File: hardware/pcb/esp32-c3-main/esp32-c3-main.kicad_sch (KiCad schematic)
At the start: 8 parts, among them J1 USB-C Receptacle USB2.0 16P

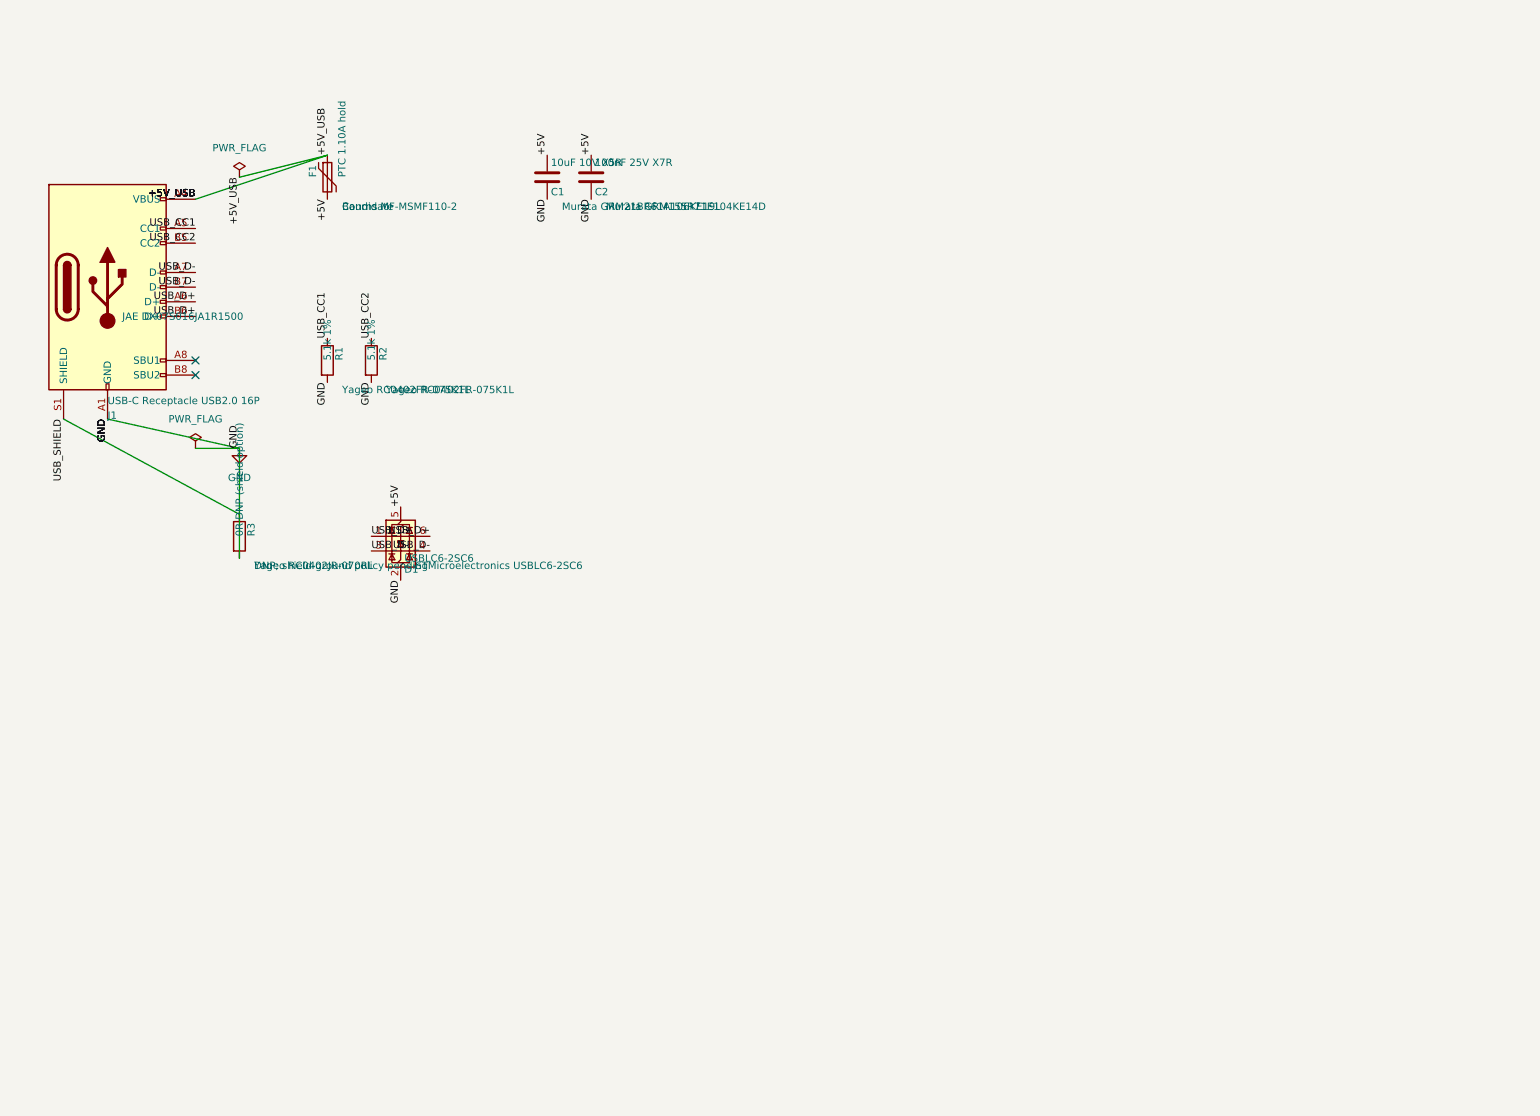
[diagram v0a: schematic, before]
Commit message: Complete ESP32-C3 main schematic
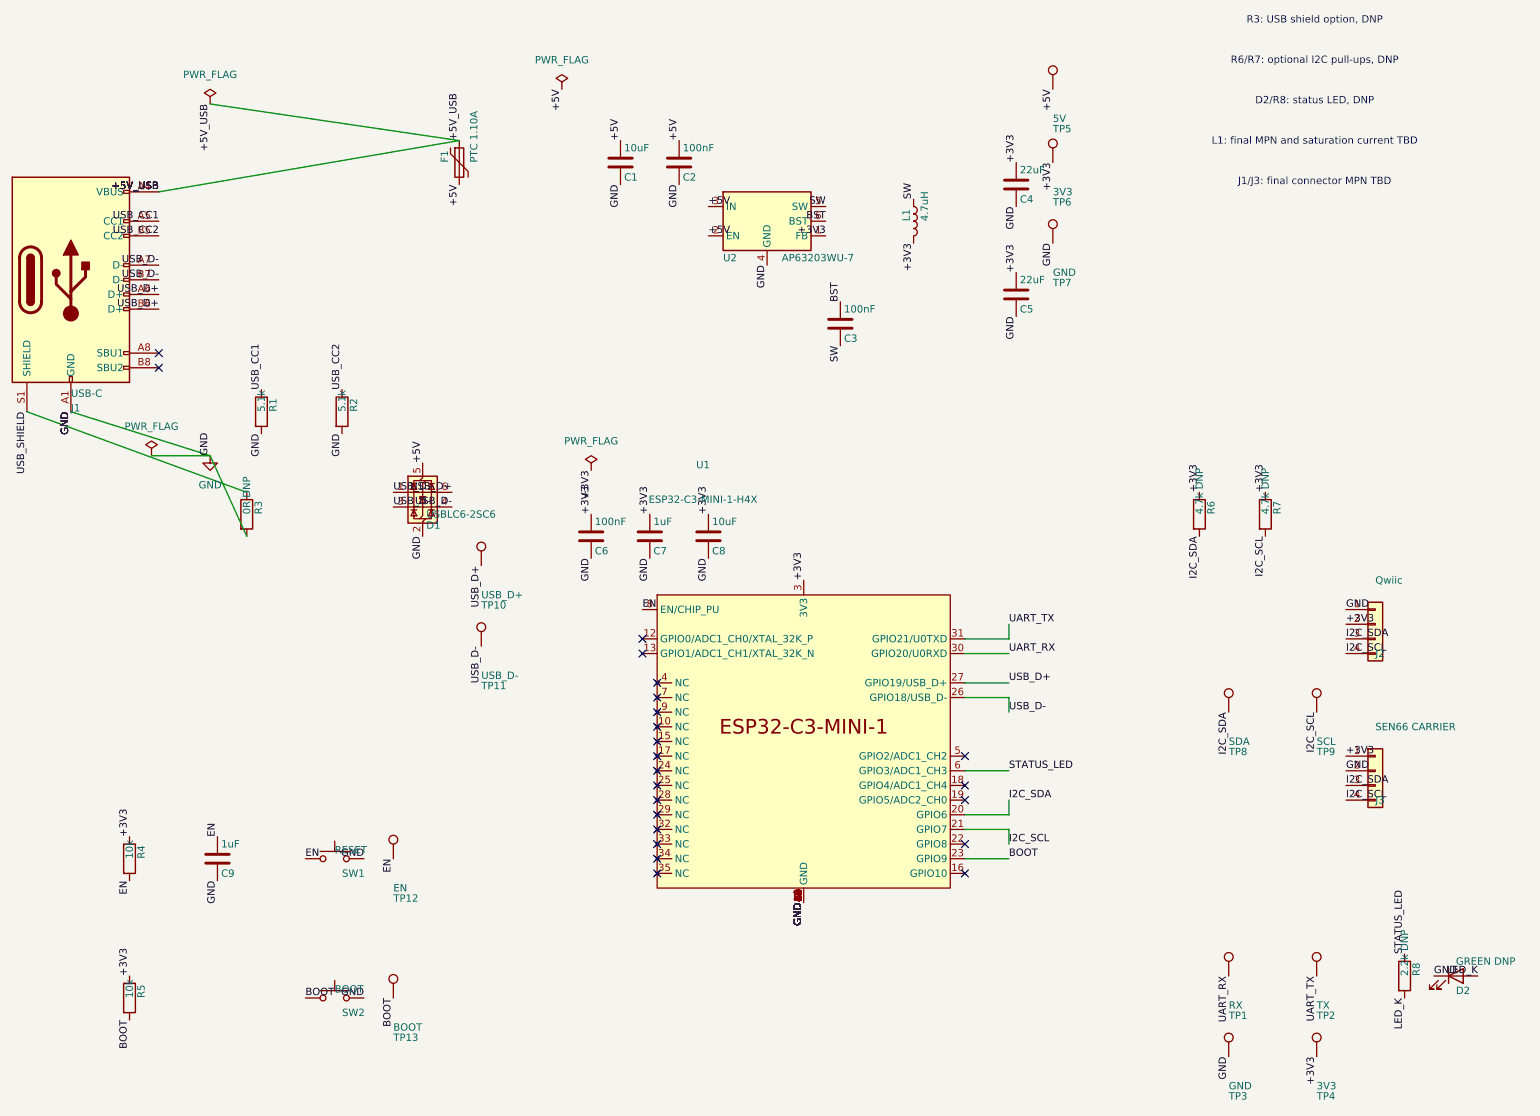
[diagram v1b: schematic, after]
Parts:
- added C3, C6: 100nF, Capacitor_SMD:C_0402_1005Metric, symbol Device:C
- added C4, C5: 22uF, Capacitor_SMD:C_0805_2012Metric, symbol Device:C
- added C7, C9: 1uF, Capacitor_SMD:C_0402_1005Metric, symbol Device:C
- added C8: 10uF, Capacitor_SMD:C_0805_2012Metric, symbol Device:C
- added D2: GREEN DNP, LED_SMD:LED_0603_1608Metric, symbol Device:LED
- added J2: Qwiic, Connector_JST:JST_SH_SM04B-SRSS-TB_1x04-1MP_P1.00mm_Horizontal, symbol Connector_Generic:Conn_01x04
- added J3: SEN66 CARRIER, Connector_PinHeader_2.54mm:PinHeader_1x04_P2.54mm_Horizontal, symbol Connector_Generic:Conn_01x04
- added L1: 4.7uH, Inductor_SMD:L_Vishay_IHLP-2020, symbol Device:L
- added R4, R5: 10k, Resistor_SMD:R_0402_1005Metric, symbol Device:R
- added R6, R7: 4.7k DNP, Resistor_SMD:R_0402_1005Metric, symbol Device:R
- added R8: 2.2k DNP, Resistor_SMD:R_0402_1005Metric, symbol Device:R
- added SW1: RESET, Button_Switch_SMD:SW_SPST_B3U-1000P, symbol Switch:SW_Push
- added SW2: BOOT, Button_Switch_SMD:SW_SPST_B3U-1000P, symbol Switch:SW_Push
- added TP1: RX, TestPoint:TestPoint_Pad_D2.0mm, symbol Connector:TestPoint
- added TP10: USB_D+, TestPoint:TestPoint_Pad_D2.0mm, symbol Connector:TestPoint
- added TP11: USB_D-, TestPoint:TestPoint_Pad_D2.0mm, symbol Connector:TestPoint
- added TP12: EN, TestPoint:TestPoint_Pad_D2.0mm, symbol Connector:TestPoint
- added TP13: BOOT, TestPoint:TestPoint_Pad_D2.0mm, symbol Connector:TestPoint
- added TP2: TX, TestPoint:TestPoint_Pad_D2.0mm, symbol Connector:TestPoint
- added TP3, TP7: GND, TestPoint:TestPoint_Pad_D2.0mm, symbol Connector:TestPoint
- added TP4, TP6: 3V3, TestPoint:TestPoint_Pad_D2.0mm, symbol Connector:TestPoint
- added TP5: 5V, TestPoint:TestPoint_Pad_D2.0mm, symbol Connector:TestPoint
- added TP8: SDA, TestPoint:TestPoint_Pad_D2.0mm, symbol Connector:TestPoint
- added TP9: SCL, TestPoint:TestPoint_Pad_D2.0mm, symbol Connector:TestPoint
- added U1: ESP32-C3-MINI-1-H4X, Espressif:ESP32-C3-MINI-1, symbol Espressif:ESP32-C3-MINI-1
- added U2: AP63203WU-7, Package_TO_SOT_SMD:TSOT-23-6, symbol Regulator_Switching:AP63203WU
- C1: value 10uF 10V X5R -> 10uF
- C2: value 100nF 25V X7R -> 100nF
- D1: LCSC (none) -> C7519
- F1: value PTC 1.10A hold -> PTC 1.10A; Status Candidate -> Candidate; JLC verification required
- J1: value USB-C Receptacle USB2.0 16P -> USB-C; LCSC (none) -> TBD
- R1, R2: value 5.1k 1% -> 5.1k
- R3: value 0R DNP (shield option) -> 0R DNP; Status DNP; shield-ground policy pending -> DNP
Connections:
- net +5V: now also TP5.1, U2.2 (EN), U2.3 (IN)
- net GND: now also C4.2, C5.2, C6.2, C7.2, C8.2, C9.2, D2.1 (K), J2.1 (Pin_1), J3.2 (Pin_2), SW1.2, SW2.2, TP3.1, TP7.1, U1.1 (GND), U1.11 (GND), U1.14 (GND), U1.2 (GND), U1.36 (GND), U1.37 (GND), U1.38 (GND), U1.39 (GND), U1.40 (GND), U1.41 (GND), U1.42 (GND), U1.43 (GND), U1.44 (GND), U1.45 (GND), U1.46 (GND), U1.47 (GND), U1.48 (GND), U1.49 (GND), U1.50 (GND), U1.51 (GND), U1.52 (GND), U1.53 (GND), U2.4 (GND)
- net USB_D+: now also TP10.1, U1.27 (GPIO19/USB_D+)
- net USB_D-: now also TP11.1, U1.26 (GPIO18/USB_D-)
- new net +3V3: C4.1, C5.1, C6.1, C7.1, C8.1, J2.2 (Pin_2), J3.1 (Pin_1), L1.2, R4.1, R5.1, R6.1, R7.1, TP4.1, TP6.1, U1.3 (3V3), U2.1 (FB)
- new net BOOT: R5.2, SW2.1, TP13.1, U1.23 (GPIO9)
- new net BST: C3.1, U2.6 (BST)
- new net EN: C9.1, R4.2, SW1.1, TP12.1, U1.8 (EN/CHIP_PU)
- new net I2C_SCL: J2.4 (Pin_4), J3.4 (Pin_4), R7.2, TP9.1, U1.21 (GPIO7)
- new net I2C_SDA: J2.3 (Pin_3), J3.3 (Pin_3), R6.2, TP8.1, U1.20 (GPIO6)
- new net LED_K: D2.2 (A), R8.2
- new net STATUS_LED: R8.1, U1.6 (GPIO3/ADC1_CH3)
- new net SW: C3.2, L1.1, U2.5 (SW)
- new net UART_RX: TP1.1, U1.30 (GPIO20/U0RXD)
- new net UART_TX: TP2.1, U1.31 (GPIO21/U0TXD)
- no-connect marks 2 -> 23
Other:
- note added: "D2/R8: status LED, DNP"
- note added: "J1/J3: final connector MPN TBD"
- note added: "L1: final MPN and saturation current TBD"
- note added: "R3: USB shield option, DNP"
- note added: "R6/R7: optional I2C pull-ups, DNP"
- company: (none) -> OMK

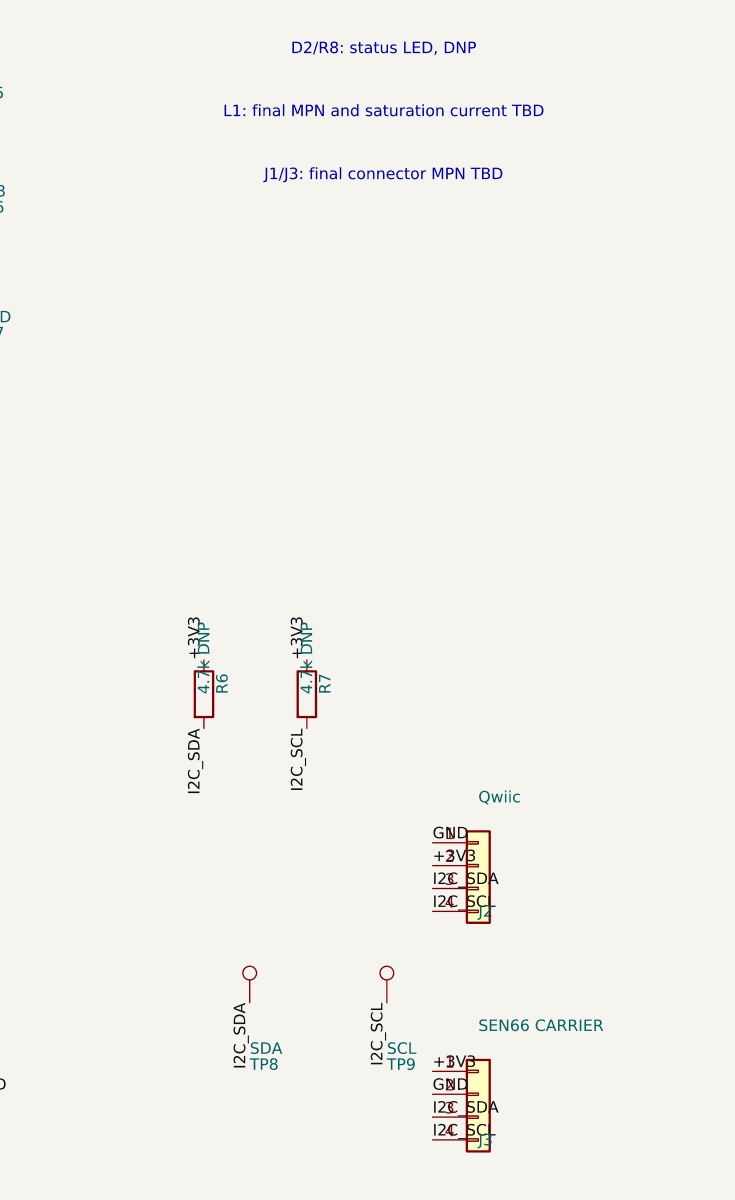
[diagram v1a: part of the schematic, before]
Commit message: Integrate JST PH connectors into schematics
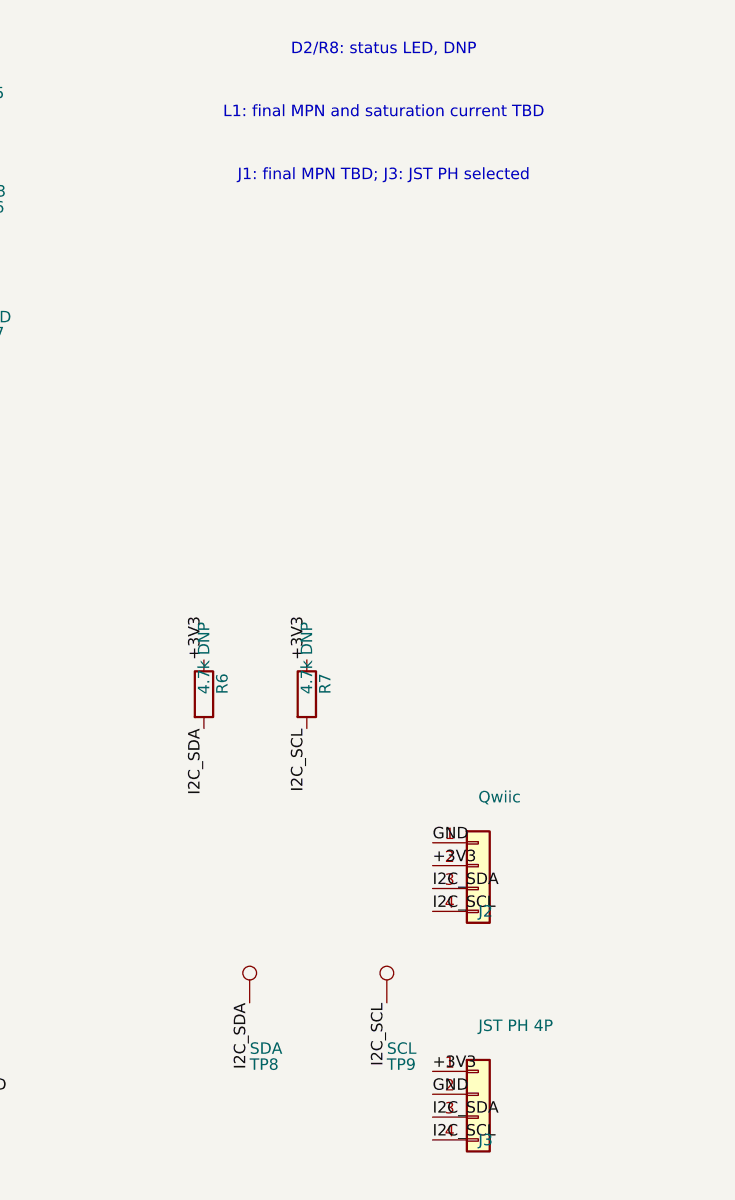
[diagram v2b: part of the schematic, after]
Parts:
- J3: value SEN66 CARRIER -> JST PH 4P; footprint Connector_PinHeader_2.54mm:PinHeader_1x04_P2.54mm_Horizontal -> Connector_JST:JST_PH_S4B-PH-K_1x04_P2.00mm_Horizontal; Assembly (none) -> TH / hand solder or wave solder candidate; LCSC (none) -> C157926; Manufacturer (none) -> JST; Manufacturer Part Number TBD -> S4B-PH-K-S(LF)(SN); Notes (none) -> Side-entry, keyed; carrier J2 matching; Status Manual solder; 2.54mm RA candidate -> Selected; manufacturing release blocked
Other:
- note added: "J1: final MPN TBD; J3: JST PH selected"
- note removed: "J1/J3: final connector MPN TBD"
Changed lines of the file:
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@@
 			)
 		)
-		(property "Value" "SEN66 CARRIER"
+		(property "Value" "JST PH 4P"
 			(at 270.51 152.4 0.0000)
 			(effects
@@
 			)
 		)
-		(property "Footprint" "Connector_PinHeader_2.54mm:PinHeader_1x04_P2.54mm_Horizontal"
+		(property "Footprint" "Connector_JST:JST_PH_S4B-PH-K_1x04_P2.00mm_Horizontal"
 			(at 270.51 160.02 0.0000)
 			(effects
@@
 			)
 		)
-		(property "Status" "Manual solder; 2.54mm RA candidate"
+		(property "Manufacturer" "JST"
 			(at 273.05 165.0999 0)
 			(effects
@@
 			)
 		)
-		(property "Manufacturer Part Number" "TBD"
+		(property "LCSC" "C157926"
+			(at 273.05 165.0999 0)
+			(effects
+				(font
+					(size 1.27 1.27)
+				)
+				(hide yes)
+			)
+		)
+		(property "Assembly" "TH / hand solder or wave solder candidate"
+			(at 273.05 165.0999 0)
+			(effects
+				(font
+					(size 1.27 1.27)
+				)
+				(hide yes)
+			)
+		)
+		(property "Status" "Selected; manufacturing release blocked"
+			(at 273.05 165.0999 0)
+			(effects
+				(font
+					(size 1.27 1.27)
+				)
+				(hide yes)
+			)
+		)
+		(property "Notes" "Side-entry, keyed; carrier J2 matching"
+			(at 273.05 165.0999 0)
+			(effects
+				(font
+					(size 1.27 1.27)
+				)
+				(hide yes)
+			)
+		)
+		(property "Manufacturer Part Number" "S4B-PH-K-S(LF)(SN)"
 			(at 273.05 165.0999 0)
 			(effects
@@
 		)
 	)
-	(text "J1/J3: final connector MPN TBD"
+	(text "J1: final MPN TBD; J3: JST PH selected"
 		(exclude_from_sim no)
 		(at 260 58 0.0000)

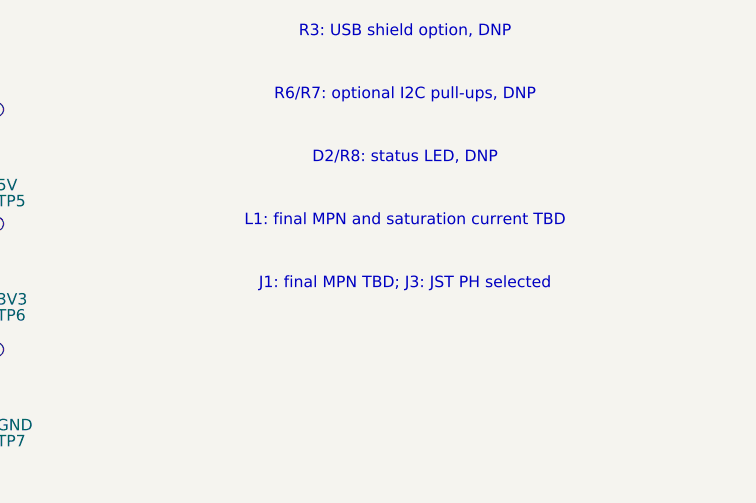
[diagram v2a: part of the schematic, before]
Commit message: Integrate XGL4020 inductor into main schematic
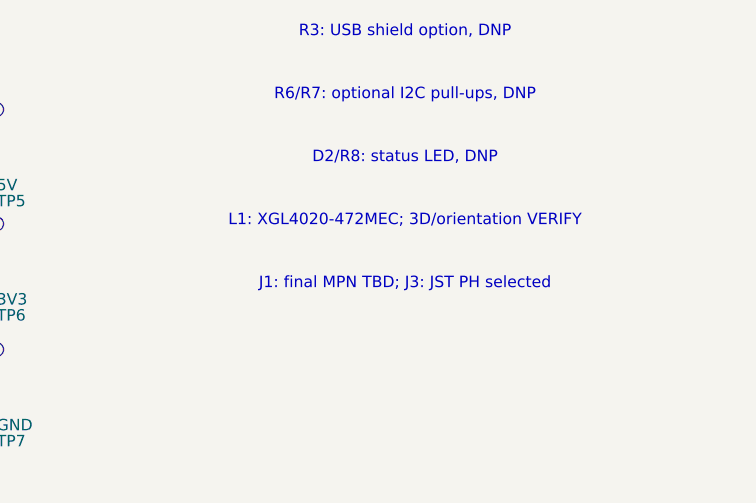
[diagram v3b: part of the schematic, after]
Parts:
- L1: footprint Inductor_SMD:L_Vishay_IHLP-2020 -> Inductor_SMD:L_Coilcraft_XxL4020; Assembly (none) -> SMT / PCBA candidate; LCSC (none) -> C6012418; Manufacturer (none) -> Coilcraft; Manufacturer Part Number TBD -> XGL4020-472MEC; Notes (none) -> 3D/start-lead orientation and procurement verify before rel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; Status Inductor candidate pending saturation-current verification -> Selected; 2D footprint accepted; manufacturing release bloc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
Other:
- note added: "L1: XGL4020-472MEC; 3D/orientation VERIFY"
- note removed: "L1: final MPN and saturation current TBD"
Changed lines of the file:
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@@
 			)
 		)
-		(property "Footprint" "Inductor_SMD:L_Vishay_IHLP-2020"
+		(property "Footprint" "Inductor_SMD:L_Coilcraft_XxL4020"
 			(at 190.5 64.77 0.0000)
 			(effects
@@
 			)
 		)
-		(property "Status" "Inductor candidate pending saturation-current verification"
+		(property "Manufacturer" "Coilcraft"
 			(at 193.04 69.8499 0)
 			(effects
@@
 			)
 		)
-		(property "Manufacturer Part Number" "TBD"
+		(property "LCSC" "C6012418"
+			(at 193.04 69.8499 0)
+			(effects
+				(font
+					(size 1.27 1.27)
+				)
+				(hide yes)
+			)
+		)
+		(property "Assembly" "SMT / PCBA candidate"
+			(at 193.04 69.8499 0)
+			(effects
+				(font
+					(size 1.27 1.27)
+				)
+				(hide yes)
+			)
+		)
+		(property "Status" "Selected; 2D footprint accepted; manufacturing release blocked"
+			(at 193.04 69.8499 0)
+			(effects
+				(font
+					(size 1.27 1.27)
+				)
+				(hide yes)
+			)
+		)
+		(property "Notes" "3D/start-lead orientation and procurement verify before release"
+			(at 193.04 69.8499 0)
+			(effects
+				(font
+					(size 1.27 1.27)
+				)
+				(hide yes)
+			)
+		)
+		(property "Manufacturer Part Number" "XGL4020-472MEC"
 			(at 193.04 69.8499 0)
 			(effects
@@
 		)
 	)
-	(text "L1: final MPN and saturation current TBD"
+	(text "L1: XGL4020-472MEC; 3D/orientation VERIFY"
 		(exclude_from_sim no)
 		(at 260 51 0.0000)
